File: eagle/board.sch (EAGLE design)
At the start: 13 parts, among them IC1 A1202UA

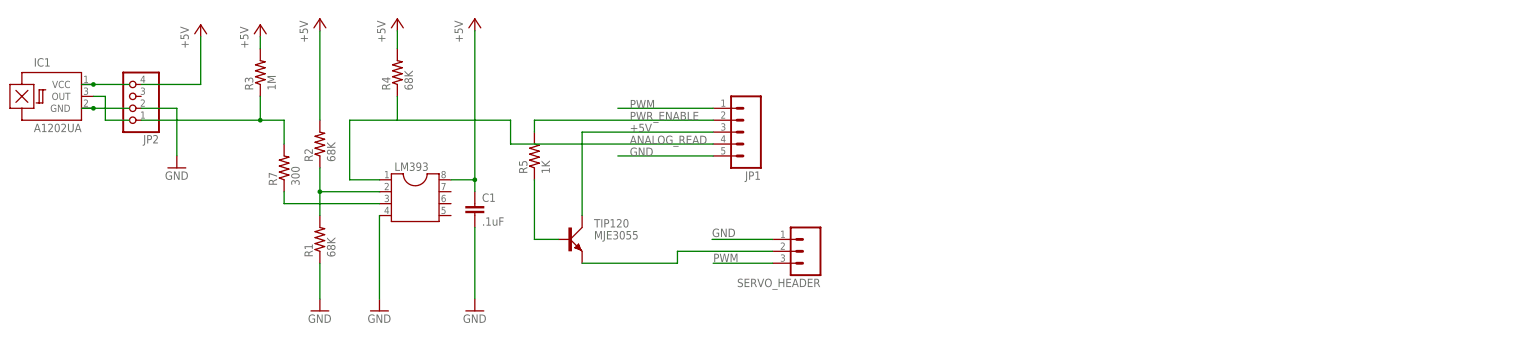
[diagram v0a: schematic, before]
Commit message: updated schematic, changed sketch to reflect board changes
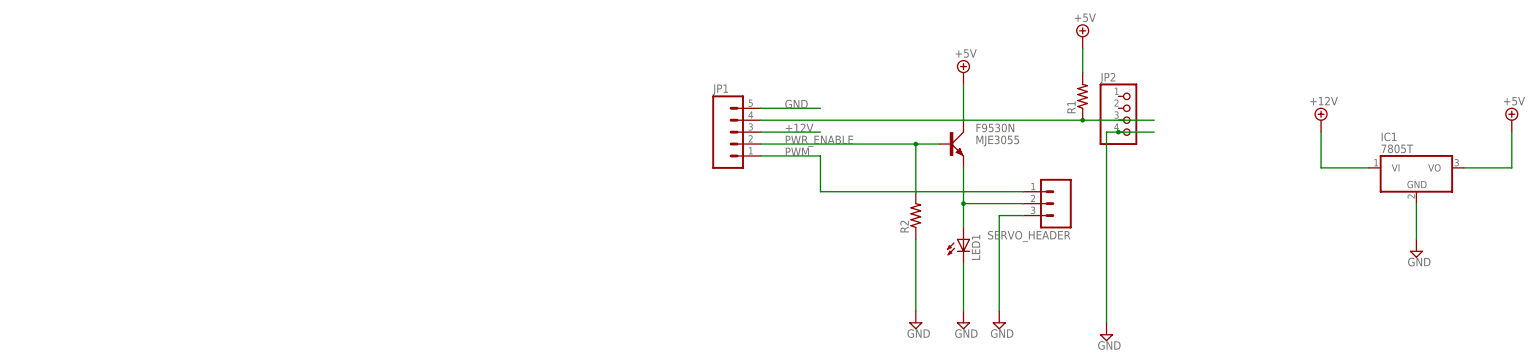
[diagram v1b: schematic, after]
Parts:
- removed C1: .1uF, SparkFun-Passives:CAP0402-CAP
- removed LM393: (no value), ic-package:DIL8
- removed R3: 1M, SparkFun-Passives:RESISTOR1206
- removed R4: 68K, SparkFun-Passives:RESISTOR1206
- removed R5: 1K, SparkFun-Passives:RESISTOR1206
- removed R7: 300, SparkFun-Passives:RESISTOR1206
- removed TIP120: MJE3055, transistor-power:MJE3055
- added F9530N: MJE3055, transistor-power:MJE3055
- added LED1: (no value), led:LED
- IC1: value A1202UA -> 7805T; device allegro:A1202UA -> linear:7805T
- R1, R2: value 68K -> (none); device SparkFun-Passives:RESISTOR1206 -> rcl:R-US_0204/7
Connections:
- removed net +5V_SWITCHED: SERVO_HEADER.2, TIP120.E
- removed net 2: R5.1, TIP120.B
- removed net ANALOG_READ: JP1.4, LM393.1, R4.1
- removed net N$2: JP2.1, R3.1, R7.2
- removed net N$5: LM393.3, R7.1
- removed net N$6: IC1.VCC
- removed net N$7: IC1.GND
- removed net N$8: IC1.OUT
- new net +12V: IC1.VI, JP1.3
- new net N$3: JP1.4, R1.1
- net +5V: now also F9530N.C, IC1.VO, R1.2; no longer C1.1, JP1.3, JP2.4, LM393.8, R2.2, R3.2, R4.2, TIP120.C
- net GND: now also IC1.GND, JP2.4, LED1.C, R2.1, SERVO_HEADER.3; no longer C1.2, JP2.2, LM393.4, R1.1, SERVO_HEADER.1
- net N$1: now also F9530N.E, LED1.A, SERVO_HEADER.2; no longer LM393.2, R1.2, R2.1
- net PWM: now also SERVO_HEADER.1; no longer SERVO_HEADER.3
- net PWR_ENABLE: now also F9530N.B, R2.2; no longer R5.2
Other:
- moved on the sheet: JP1, JP2, R1, R2, SERVO_HEADER
